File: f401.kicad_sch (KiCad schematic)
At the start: 22 parts, among them J18 Conn_01x01_Socket, J21 Conn_01x04, SW1 SW_Push, SW2 SW_Push, U5 STM32F401CCUx / UFQFPN48, Y1 25MHz, Y2 32.758kHz

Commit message: ongoing add MCU and radio.
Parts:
- C10, C11, C12, C13, C14, C17, C9: MountType (none) -> SMT
- D1: footprint (none) -> ProjectLib:LED_0603_1608Metric; symbol Device:LED -> ProjectLib:LED; Manufacturer (none) -> Yongyu Photoelectric; MfgPart (none) -> yy0603re-nn1s0-t2ar4; MountType (none) -> SMT; Notes (none) -> or equivalent
- D2: footprint (none) -> ProjectLib:LED_0603_1608Metric; symbol Device:LED -> ProjectLib:LED; Manufacturer (none) -> Yongyu Photoelectric; MfgPart (none) -> yy0603bl-nn1s0-t2ar4; MountType (none) -> SMT; Notes (none) -> or equivalent
- J18: value Conn_01x01_Socket -> THTPad; footprint (none) -> ProjectLib:TestPoint_THTPad_D1.0mm_Drill0.5mm; MountType (none) -> PTH; now not fitted
- J21: value Conn_01x04 -> Conn_01x04_Pin; footprint (none) -> ProjectLib:JST_XH_B4B-XH-A_1x04_P2.50mm_Vertical; symbol Connector_Generic:Conn_01x04 -> ProjectLib:Conn_01x04_Pin; MountType (none) -> PTH
- L1: value 2uH -> 2.2uH; footprint (none) -> ProjectLib:L_TDK_MLZ1608; symbol Device:L -> ProjectLib:L; Manufacturer (none) -> TDK; MfgPart (none) -> MLZ1608N2R2LT000; MountType (none) -> SMT; Notes (none) -> or equivalent
- R23, R24: footprint (none) -> ProjectLib:R_0603_1608Metric; symbol Device:R -> ProjectLib:R_US; MountType (none) -> SMT
- R25, R26: value 10K -> 10K 1%; footprint (none) -> ProjectLib:R_0603_1608Metric; symbol Device:R -> ProjectLib:R_US; MountType (none) -> SMT
- R27: value 10k -> 10k 1%; footprint (none) -> ProjectLib:R_0603_1608Metric; symbol Device:R -> ProjectLib:R_US; MountType (none) -> SMT
- SW1, SW2: footprint (none) -> ProjectLib:SW_SPST_B3U-1000P; symbol Switch:SW_Push -> ProjectLib:SW_Push; Manufacturer (none) -> Omron; MfgPart (none) -> B3U-1000P; MountType (none) -> SMT
- U5: symbol MCU_ST_STM32F4:STM32F401CCUx -> ProjectLib:STM32F401CCUx; MountType (none) -> SMT
- Y1, Y2: symbol Device:Crystal -> ProjectLib:Crystal; MountType (none) -> SMT; Notes (none) -> or equivalent
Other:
- moved on the sheet: L1

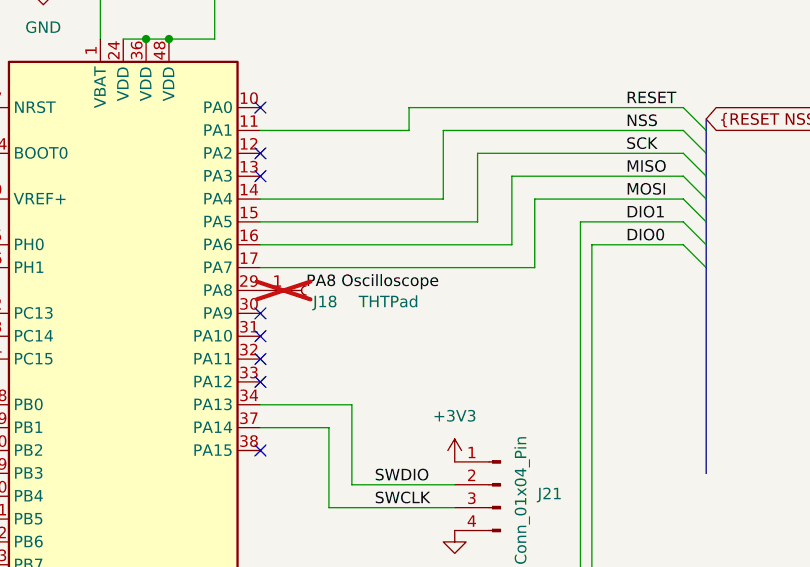
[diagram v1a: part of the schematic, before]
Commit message: ERC passing, Crytals not specified. Considering reverse polarity safeguard.
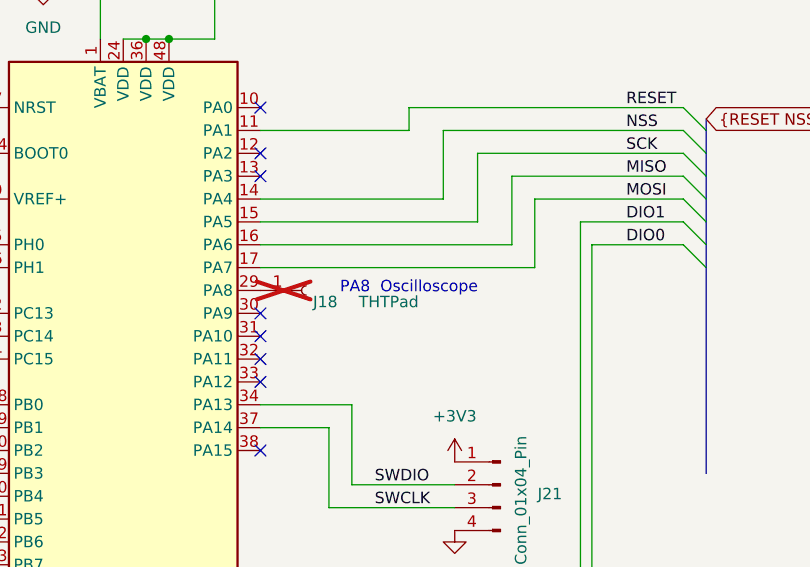
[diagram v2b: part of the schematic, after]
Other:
- note added: "PA8 Oscilloscope"
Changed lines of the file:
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@@
 		)
 	)
-	(label "PA8  Oscilloscope"
-		(at 162.56 73.66 0)
+	(text "PA8  Oscilloscope"
+		(exclude_from_sim no)
+		(at 173.99 73.406 0)
 		(effects
 			(font
 				(size 1.27 1.27)
 			)
-			(justify left bottom)
 		)
 	)

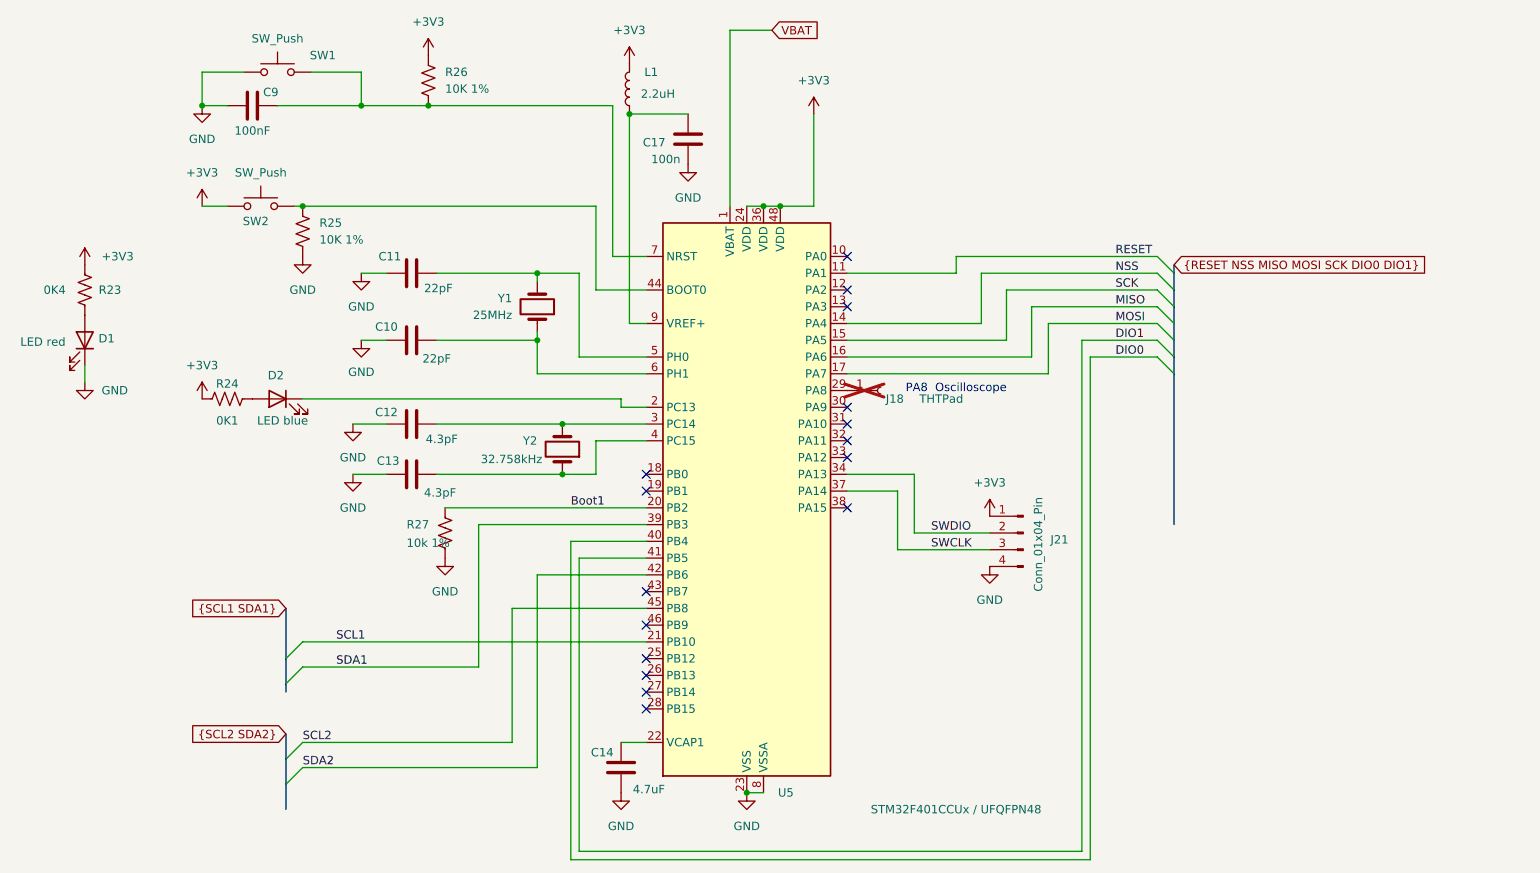
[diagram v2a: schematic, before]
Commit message: f401.kicad_sch mostly complete other than xtals. Considering switch to f411 for memory, FPU, and generation 2 oscillator that gives better crystal choices.
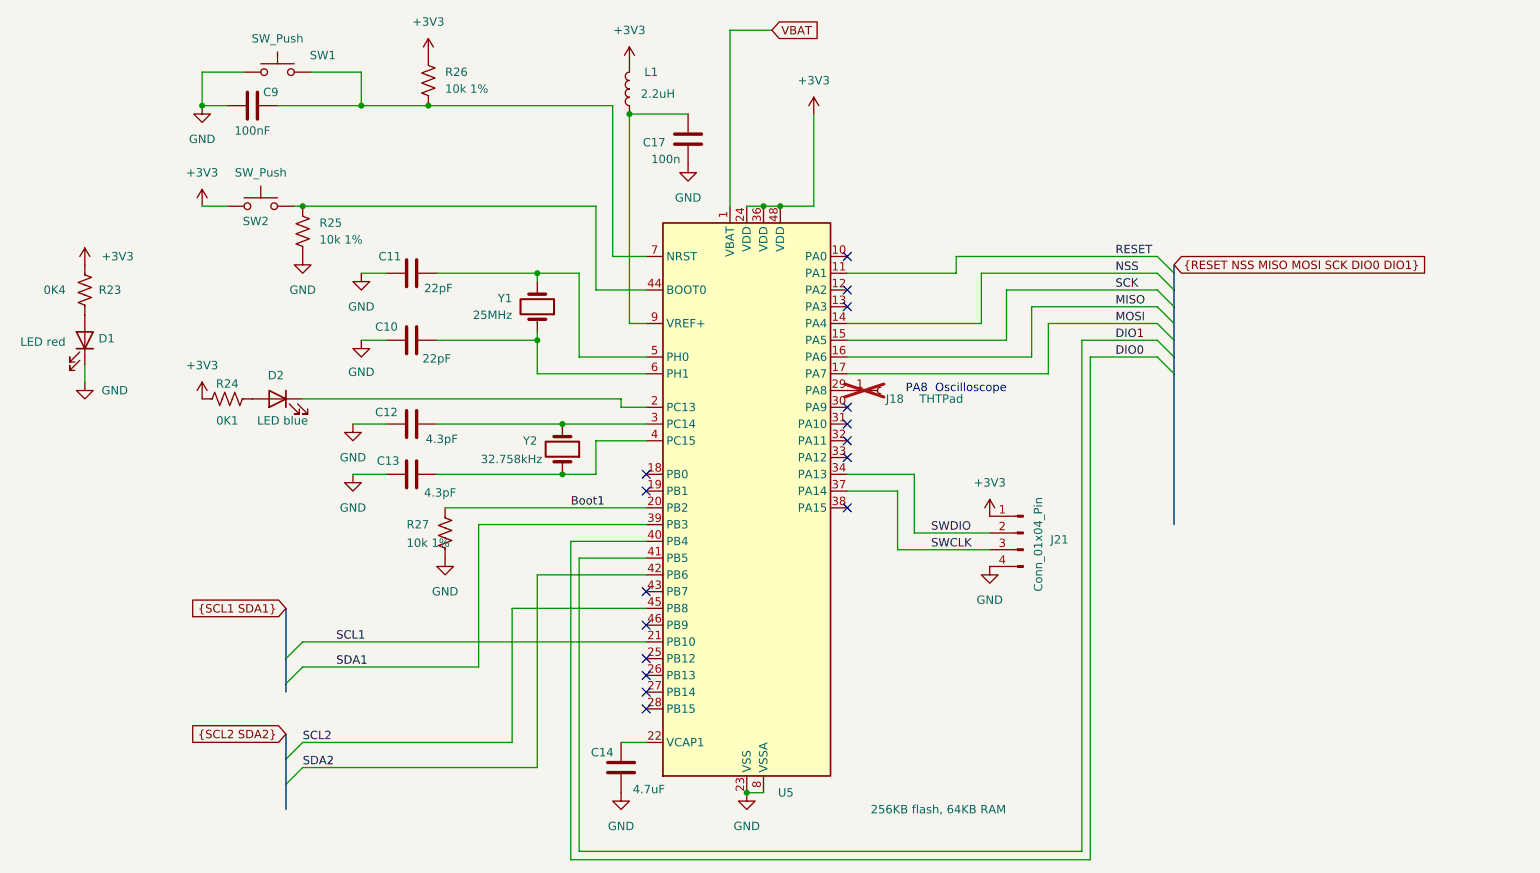
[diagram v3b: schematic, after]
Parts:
- R23, R24, R27: footprint ProjectLib:R_0603_1608Metric -> ProjectLib:R_0201_0603Metric
- R25, R26: value 10K 1% -> 10k 1%; footprint ProjectLib:R_0603_1608Metric -> ProjectLib:R_0201_0603Metric
- U5: value STM32F401CCUx / UFQFPN48 -> 256KB flash, 64KB RAM; Manufacturer (none) -> STMicroelectronics; MfgPart (none) -> STM32F401CCUx / UFQFPN48
- Y1, Y2: Notes or equivalent -> (none)
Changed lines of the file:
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@@
 			)
 		)
-		(property "Footprint" "ProjectLib:R_0603_1608Metric"
+		(property "Footprint" "ProjectLib:R_0201_0603Metric"
 			(at 94.742 95.25 90)
 			(effects
@@
 			)
 		)
-		(property "Notes" "or equivalent"
+		(property "Notes" ""
 			(at 110.49 60.96 0)
 			(effects
@@
 			)
 		)
-		(property "Footprint" "ProjectLib:R_0603_1608Metric"
+		(property "Footprint" "ProjectLib:R_0201_0603Metric"
 			(at 63.5 76.708 90)
 			(effects
@@
 			)
 		)
-		(property "Footprint" "ProjectLib:R_0603_1608Metric"
+		(property "Footprint" "ProjectLib:R_0201_0603Metric"
 			(at 40.132 58.42 90)
 			(effects
@@
 			)
 		)
-		(property "Value" "10K 1%"
+		(property "Value" "10k 1%"
 			(at 96.52 27.9399 0)
 			(effects
@@
 			)
 		)
-		(property "Footprint" "ProjectLib:R_0603_1608Metric"
+		(property "Footprint" "ProjectLib:R_0201_0603Metric"
 			(at 92.202 26.67 90)
 			(effects
@@
 			)
 		)
-		(property "Value" "10K 1%"
+		(property "Value" "10k 1%"
 			(at 77.47 50.7999 0)
 			(effects
@@
 			)
 		)
-		(property "Footprint" "ProjectLib:R_0603_1608Metric"
+		(property "Footprint" "ProjectLib:R_0201_0603Metric"
 			(at 73.152 49.53 90)
 			(effects
@@
 			)
 		)
-		(property "Value" "STM32F401CCUx / UFQFPN48"
+		(property "Value" "256KB flash,  64KB RAM"
 			(at 161.036 137.16 0)
 			(effects
@@
 			)
 		)
-		(property "Description" "STMicroelectronics Arm Cortex-M4 MCU, 256KB flash, 64KB RAM, 84 MHz, 1.7-3.6V, 36 GPIO, UFQFPN48"
+		(property "Description" "STMicroelectronics Arm Cortex-M4 MCU,  84 MHz, 1.7-3.6V, 36 GPIO, UFQFPN48"
 			(at 142.24 91.44 0)
 			(effects
@@
 		)
 		(property "MountType" "SMT"
+			(at 142.24 91.44 0)
+			(effects
+				(font
+					(size 1.27 1.27)
+				)
+				(hide yes)
+			)
+		)
+		(property "Manufacturer" "STMicroelectronics"
+			(at 142.24 91.44 0)
+			(effects
+				(font
+					(size 1.27 1.27)
+				)
+				(hide yes)
+			)
+		)
+		(property "MfgPart" "STM32F401CCUx / UFQFPN48"
 			(at 142.24 91.44 0)
 			(effects
@@
 			)
 		)
-		(property "Notes" "or equivalent"
+		(property "Notes" ""
 			(at 114.3 82.55 0)
 			(effects
